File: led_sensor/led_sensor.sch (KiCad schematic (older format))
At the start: 45 parts

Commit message: Reset_Line
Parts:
- added C1: 1u, SamacSys_Parts:CAPC1005X55N, symbol Device:C_Small
- added R1, R2, R3, R4, R5, R6, R7, R8: 10k, SamacSys_Parts:RESC1608X55N, symbol Device:R
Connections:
- net +3V3: now also C1.1, R1.1, R2.1, R4.1, R5.1, R6.1, R7.1, R8.1
- net GND: now also C1.2
- net at HM#1.1 (D3), U#3.3 (Hout): now also R4.2
- net at H#7.3 (Hout), HM#1.12 (D7): now also R8.2
- net at HM#1.13 (D6), U#6.3 (Hout): now also R7.2
- net at HM#1.14 (D5), U#5.3 (Hout): now also R6.2
- net at HM#1.15 (D4), U#4.3 (Hout): now also R5.2
- net at HM#1.2 (D2), U#2.3 (Hout): now also R3.2
- net at HM#1.3 (D1), U#1.3 (Hout): now also R2.2
- net at H#0.3 (Hout), HM#1.4 (D0): now also R1.2
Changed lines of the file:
@@
 U 1 1 615A38AC
 P 4750 3350
-F 0 "H#0" H 4825 3365 50  0000 C CNN
-F 1 "AH3362Q" H 4825 3274 50  0000 C CNN
+F 0 "H#0" V 4700 3150 20  0000 C CNN
+F 1 "AH3362Q" V 4700 2900 20  0000 C CNN
 F 2 "Hall:AH3662Q" H 4750 3350 50  0001 C CNN
 F 3 "" H 4750 3350 50  0001 C CNN
@@
 U 1 1 615A5ADB
 P 5500 3350
-F 0 "U#1" H 5575 3365 50  0000 C CNN
-F 1 "AH3362Q" H 5575 3274 50  0000 C CNN
+F 0 "U#1" V 5450 3150 20  0000 C CNN
+F 1 "AH3362Q" V 5450 2900 20  0000 C CNN
 F 2 "Hall:AH3662Q" H 5500 3350 50  0001 C CNN
 F 3 "" H 5500 3350 50  0001 C CNN
@@
 U 1 1 615A5DEF
 P 6150 3350
-F 0 "U#2" H 6225 3365 50  0000 C CNN
-F 1 "AH3362Q" H 6225 3274 50  0000 C CNN
+F 0 "U#2" V 6100 3100 50  0000 C CNN
+F 1 "AH3362Q" V 6100 2900 20  0000 C CNN
 F 2 "Hall:AH3662Q" H 6150 3350 50  0001 C CNN
 F 3 "" H 6150 3350 50  0001 C CNN
@@
 U 1 1 615A6E92
 P 8200 3350
-F 0 "U#5" H 8275 3365 50  0000 C CNN
-F 1 "AH3362Q" H 8275 3274 50  0000 C CNN
+F 0 "U#5" H 8300 3350 50  0000 C CNN
+F 1 "AH3362Q" H 8250 3250 50  0000 C CNN
 F 2 "Hall:AH3662Q" H 8200 3350 50  0001 C CNN
 F 3 "" H 8200 3350 50  0001 C CNN
@@
 	6450 3150 5800 3150
 Connection ~ 5800 3150
-Wire Wire Line
-	5800 3150 5150 3150
 Connection ~ 5150 3150
-Wire Wire Line
-	5150 3150 4400 3150
 Connection ~ 4400 3150
 Wire Wire Line
@@
 	4100 1750 4100 3800
 Wire Wire Line
-	4100 3800 4500 3800
-Wire Wire Line
 	4500 3800 4500 3700
 Wire Wire Line
@@
 	4050 3850 5250 3850
 Wire Wire Line
-	5250 3850 5250 3700
+	5250 3850 5250 3800
 Wire Wire Line
 	3200 2950 3200 1950
@@
 	4000 3900 5900 3900
 Wire Wire Line
-	5900 3900 5900 3700
-Wire Wire Line
 	3300 2950 3300 2050
 Wire Wire Line
@@
 	3950 3950 6550 3950
 Wire Wire Line
-	6550 3950 6550 3700
-Wire Wire Line
 	3200 3950 3200 4000
 Wire Wire Line
 	3200 4000 7250 4000
 Wire Wire Line
-	7250 4000 7250 3700
-Wire Wire Line
 	3100 3950 3100 4050
 Wire Wire Line
-	3100 4050 7950 4050
-Wire Wire Line
-	7950 4050 7950 3700
-Wire Wire Line
 	3000 3950 3000 4100
 Wire Wire Line
 	3000 4100 8600 4100
-Wire Wire Line
-	8600 4100 8600 3700
 $Comp
 L led_sensor-rescue:AH3362Q-HallSensor H#7
@@
 Wire Wire Line
 	2900 4150 9250 4150
-Wire Wire Line
-	9250 4150 9250 3700
 $Comp
 L led_sensor-rescue:XZCFBB53W-8VF-xzcfbb53w-8vf LED0
@@
 Connection ~ 8400 4250
 Wire Wire Line
-	8400 4250 9050 4250
+	8400 4250 8900 4250
 Wire Wire Line
 	7750 4250 7750 3700
 Connection ~ 7750 4250
 Wire Wire Line
-	7750 4250 8400 4250
+	7750 4250 8250 4250
 Wire Wire Line
 	7050 4250 7050 3700
 Connection ~ 7050 4250
 Wire Wire Line
-	7050 4250 7750 4250
+	7050 4250 7550 4250
 Wire Wire Line
 	6350 4250 6350 3700
 Connection ~ 6350 4250
 Wire Wire Line
-	6350 4250 7050 4250
+	6350 4250 6850 4250
 Wire Wire Line
 	5700 3700 5700 4250
@@
 Connection ~ 5000 4250
 Wire Wire Line
-	5000 4250 5700 4250
-Wire Wire Line
-	4300 3700 4300 4250
+	5000 4250 5550 4250
 Connection ~ 4300 4250
-Wire Wire Line
-	4300 4250 5000 4250
 Connection ~ 1500 2950
 Text Label 2100 2500 1    50   ~ 0
@@
 Text Notes 8900 2150 0    197  ~ 0
 Circuit
+Wire Wire Line
+	4400 3150 5150 3150
+Wire Wire Line
+	5150 3150 5800 3150
+Wire Wire Line
+	3300 4350 3300 4600
+Connection ~ 3300 4350
+$Comp
+L Device:C_Small C1
+U 1 1 616B7A24
+P 3300 4700
+F 0 "C1" H 3392 4746 50  0000 L CNN
+F 1 "1u" H 3392 4655 50  0000 L CNN
+F 2 "SamacSys_Parts:CAPC1005X55N" H 3300 4700 50  0001 C CNN
+F 3 "~" H 3300 4700 50  0001 C CNN
+	1    3300 4700
+	1    0    0    -1
+$EndComp
+$Comp
+L power:GND #PWR0102
+U 1 1 616B8372
+P 3300 4800
+F 0 "#PWR0102" H 3300 4550 50  0001 C CNN
+F 1 "GND" H 3305 4627 50  0000 C CNN
+F 2 "" H 3300 4800 50  0001 C CNN
+F 3 "" H 3300 4800 50  0001 C CNN
+	1    3300 4800
+	1    0    0    -1
+$EndComp
+Wire Wire Line
+	4300 3700 4300 4250
+Wire Wire Line
+	3100 4050 7950 4050
+Wire Wire Line
+	4300 4250 4800 4250
+Wire Wire Line
+	4100 3800 4500 3800
+$Comp
+L Device:R R1
+U 1 1 616C2869
+P 4650 3800
+F 0 "R1" V 4443 3800 50  0000 C CNN
+F 1 "10k" V 4534 3800 50  0000 C CNN
+F 2 "SamacSys_Parts:RESC1608X55N" V 4580 3800 50  0001 C CNN
+F 3 "~" H 4650 3800 50  0001 C CNN
+	1    4650 3800
+	0    1    1    0
+$EndComp
+Connection ~ 4500 3800
+Wire Wire Line
+	4800 3800 4800 4250
+Connection ~ 4800 4250
+Wire Wire Line
+	4800 4250 5000 4250
+$Comp
+L Device:R R2
+U 1 1 616CA368
+P 5400 3800
+F 0 "R2" V 5193 3800 50  0000 C CNN
+F 1 "10k" V 5284 3800 50  0000 C CNN
+F 2 "SamacSys_Parts:RESC1608X55N" V 5330 3800 50  0001 C CNN
+F 3 "~" H 5400 3800 50  0001 C CNN
+	1    5400 3800
+	0    1    1    0
+$EndComp
+Wire Wire Line
+	5550 3800 5550 4250
+Connection ~ 5250 3800
+Wire Wire Line
+	5250 3800 5250 3700
+Connection ~ 5550 4250
+Wire Wire Line
+	5550 4250 5700 4250
+$Comp
+L Device:R R3
+U 1 1 616CF95A
+P 6050 3800
+F 0 "R3" V 5843 3800 50  0000 C CNN
+F 1 "10k" V 5934 3800 50  0000 C CNN
+F 2 "SamacSys_Parts:RESC1608X55N" V 5980 3800 50  0001 C CNN
+F 3 "~" H 6050 3800 50  0001 C CNN
+	1    6050 3800
+	0    1    1    0
+$EndComp
+Wire Wire Line
+	6200 3800 6200 4250
+$Comp
+L Device:R R4
+U 1 1 616D24BA
+P 6700 3800
+F 0 "R4" V 6493 3800 50  0000 C CNN
+F 1 "10k" V 6584 3800 50  0000 C CNN
+F 2 "SamacSys_Parts:RESC1608X55N" V 6630 3800 50  0001 C CNN
+F 3 "~" H 6700 3800 50  0001 C CNN
+	1    6700 3800
+	0    1    1    0
+$EndComp
+Wire Wire Line
+	6850 3800 6850 4250
+Connection ~ 6850 4250
+Wire Wire Line
+	6850 4250 7050 4250
+$Comp
+L Device:R R5
+U 1 1 616D7BCC
+P 7400 3800
+F 0 "R5" V 7193 3800 50  0000 C CNN
+F 1 "10k" V 7284 3800 50  0000 C CNN
+F 2 "SamacSys_Parts:RESC1608X55N" V 7330 3800 50  0001 C CNN
+F 3 "~" H 7400 3800 50  0001 C CNN
+	1    7400 3800
+	0    1    1    0
+$EndComp
+Wire Wire Line
+	7550 3800 7550 4250
+$Comp
+L Device:R R6
+U 1 1 616DA8B7
+P 8100 3800
+F 0 "R6" V 7893 3800 50  0000 C CNN
+F 1 "10k" V 7984 3800 50  0000 C CNN
+F 2 "SamacSys_Parts:RESC1608X55N" V 8030 3800 50  0001 C CNN
+F 3 "~" H 8100 3800 50  0001 C CNN
+	1    8100 3800
+	0    1    1    0
+$EndComp
+Wire Wire Line
+	8250 3800 8250 4250
+Connection ~ 7550 4250
+Wire Wire Line
+	7550 4250 7750 4250
+Connection ~ 8250 4250
+Wire Wire Line
+	8250 4250 8400 4250
+Connection ~ 9050 4250
+$Comp
+L Device:R R7
+U 1 1 616E324D
+P 8750 3800
+F 0 "R7" V 8543 3800 50  0000 C CNN
+F 1 "10k" V 8634 3800 50  0000 C CNN
+F 2 "SamacSys_Parts:RESC1608X55N" V 8680 3800 50  0001 C CNN
+F 3 "~" H 8750 3800 50  0001 C CNN
+	1    8750 3800
+	0    1    1    0
+$EndComp
+Wire Wire Line
+	8900 3800 8900 4250
+$Comp
+L Device:R R8
+U 1 1 616E6214
+P 9400 3800
+F 0 "R8" V 9193 3800 50  0000 C CNN
+F 1 "10k" V 9284 3800 50  0000 C CNN
+F 2 "SamacSys_Parts:RESC1608X55N" V 9330 3800 50  0001 C CNN
+F 3 "~" H 9400 3800 50  0001 C CNN
+	1    9400 3800
+	0    1    1    0
+$EndComp
+Wire Wire Line
+	9550 3800 9550 4250
+Wire Wire Line
+	9050 4250 9550 4250
+Wire Wire Line
+	5900 3700 5900 3800
+Connection ~ 5900 3800
+Wire Wire Line
+	5900 3800 5900 3900
+Wire Wire Line
+	6550 3700 6550 3800
+Connection ~ 6550 3800
+Wire Wire Line
+	6550 3800 6550 3950
+Wire Wire Line
+	7250 3700 7250 3800
+Connection ~ 7250 3800
+Wire Wire Line
+	7250 3800 7250 4000
+Wire Wire Line
+	7950 3700 7950 3800
+Connection ~ 7950 3800
+Wire Wire Line
+	7950 3800 7950 4050
+Wire Wire Line
+	8600 3700 8600 3800
+Connection ~ 8600 3800
+Wire Wire Line
+	8600 3800 8600 4100
+Wire Wire Line
+	9250 3700 9250 3800
+Connection ~ 9250 3800
+Wire Wire Line
+	9250 3800 9250 4150
+Connection ~ 8900 4250
+Wire Wire Line
+	8900 4250 9050 4250
 $EndSCHEMATC

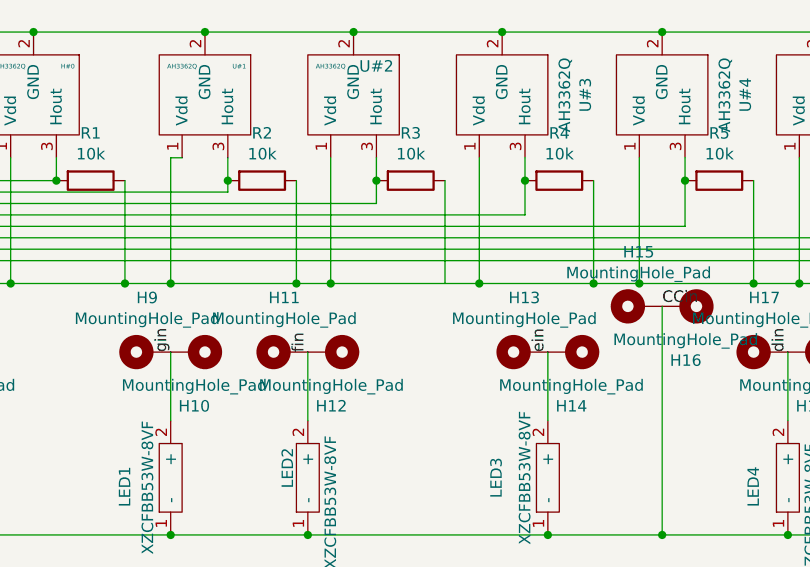
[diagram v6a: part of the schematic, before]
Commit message: Added Pullups to Daughterboard
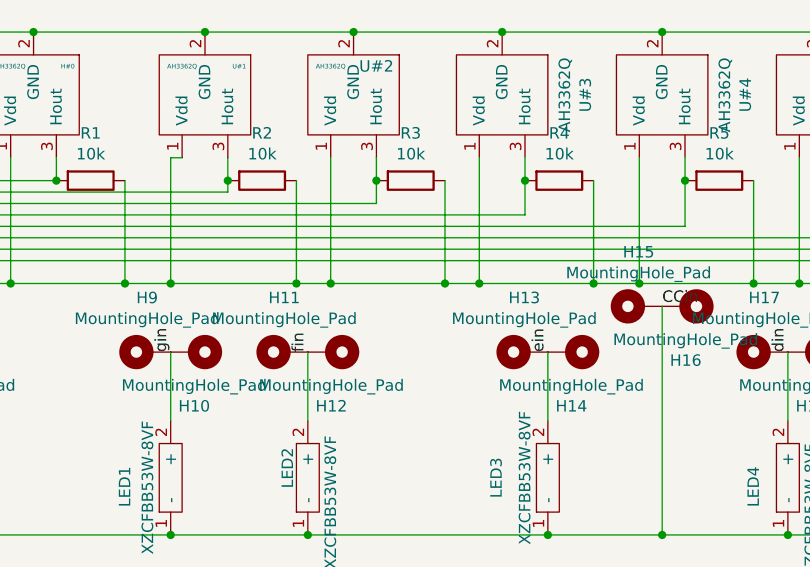
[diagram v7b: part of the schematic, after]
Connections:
- net +3V3: now also R3.1
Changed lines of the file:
@@
 Connection ~ 5700 4250
 Wire Wire Line
-	5700 4250 6350 4250
+	5700 4250 6200 4250
 Wire Wire Line
 	5000 4250 5000 3700
@@
 Wire Wire Line
 	8900 4250 9050 4250
+Connection ~ 6200 4250
+Wire Wire Line
+	6200 4250 6350 4250
 $EndSCHEMATC

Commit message: Updated Screenshots
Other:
- note added: "Daughterboard Circuit"
- note removed: "Circuit"
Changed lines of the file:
@@
 Wire Notes Line
 	700  1500 700  6000
-Text Notes 8900 2150 0    197  ~ 0
-Circuit
+Text Notes 7300 2050 0    197  ~ 0
+Daughterboard Circuit
 Wire Wire Line
 	4400 3150 5150 3150
